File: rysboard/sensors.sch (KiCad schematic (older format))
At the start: 11 parts, among them J11 PICO_BLADE_5, J13 PICO_BLADE_5, J2 PICO_BLADE_5, J3 PICO_BLADE_5, J4 PICO_BLADE_7, J5 PICO_BLADE_5, J6 PICO_BLADE_5, J7 PICO_BLADE_5, J9 PICO_BLADE_5

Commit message: rysboard: schematic cleanup done after kicad import
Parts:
- removed J11, J13, J2, J3, J6, J7, J9: PICO_BLADE_5, symbol rysboard:PICO_BLADE_5
- removed J4: PICO_BLADE_7, symbol rysboard:PICO_BLADE_7
- removed R1, R2: 10k, symbol rysboard:R--rys_PCB-SchDoc-rescue-rysboard-rescue
- added J10: ToF3, Connector_Molex:Molex_PicoBlade_53047-0510_1x05_P1.25mm_Vertical, symbol Connector_Generic:Conn_01x05
- added J11: ToF4, Connector_Molex:Molex_PicoBlade_53047-0510_1x05_P1.25mm_Vertical, symbol Connector_Generic:Conn_01x05
- added J12: ToF5, Connector_Molex:Molex_PicoBlade_53047-0510_1x05_P1.25mm_Vertical, symbol Connector_Generic:Conn_01x05
- added J13: ToF6, Connector_Molex:Molex_PicoBlade_53047-0510_1x05_P1.25mm_Vertical, symbol Connector_Generic:Conn_01x05
- added J14: SPI, Connector_Molex:Molex_PicoBlade_53047-0710_1x07_P1.25mm_Vertical, symbol Connector_Generic:Conn_01x07
- added J15: Temp, Connector_Molex:Molex_PicoBlade_53047-0510_1x05_P1.25mm_Vertical, symbol Connector_Generic:Conn_01x05
- added J16: IMU, Connector_Molex:Molex_PicoBlade_53047-0510_1x05_P1.25mm_Vertical, symbol Connector_Generic:Conn_01x05
- added J9: ToF2, Connector_Molex:Molex_PicoBlade_53047-0510_1x05_P1.25mm_Vertical, symbol Connector_Generic:Conn_01x05
- J8: renamed from J5; value PICO_BLADE_5 -> ToF1; footprint (none) -> Connector_Molex:Molex_PicoBlade_53047-0510_1x05_P1.25mm_Vertical; symbol rysboard:PICO_BLADE_5 -> Connector_Generic:Conn_01x05
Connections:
- net labels added: +3V3, I2C1_CLK, I2C1_SDA, I2C2_CLK, I2C2_SDA, IMU_IRQ, SPI_CLK, SPI_CS, SPI_IRQ, SPI_MISO, SPI_MOSI, TOF1_EN, TOF2_EN, TOF3_EN, TOF4_EN, TOF5_EN, TOF6_EN
- net labels removed: 3V3, BUSY, CE1, FLAG, IRQ, MISO, MOSI, O~D~, SCL, SCL1, SCLK, SDA, SDA1, TOF0, TOF1, TOF2, TOF3, TOF4, TOF5
- wire segments 70 -> 76
- no-connect marks 0 -> 1
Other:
- note added: "6x ToF I2C connector"
- note added: "External SPI connector"
- note added: "I2C IMU connector"
- note added: "I2C temperature sensor connector"
- note removed: "Złącze I2C IMU"
- note removed: "Złącze I2C TEMP"
- note removed: "Złącze I2C ToF 6x"
- note removed: "Złącze SPI"

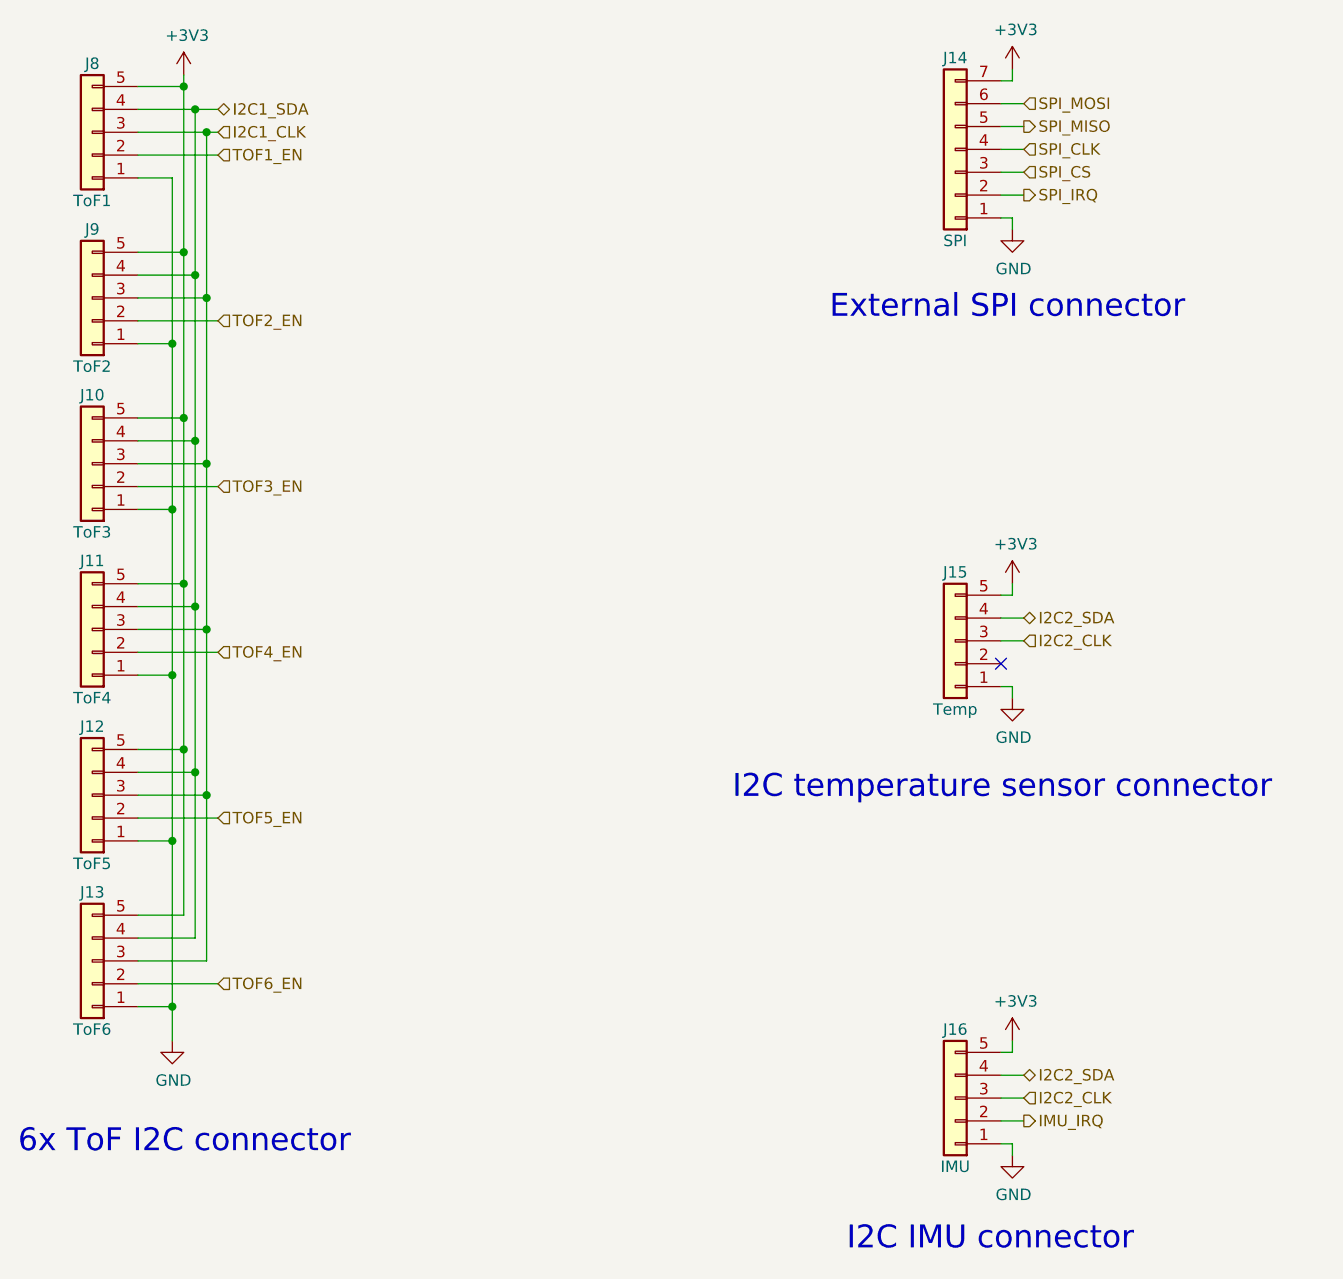
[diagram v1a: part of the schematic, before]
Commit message: rysboard: 4.2 schematic
Change the I2C buses and GPIOs used
Fix L6470 connections
Change ADC to 4-channel
Add 2 user LEDs
Add I2C pullups
Add serial connector
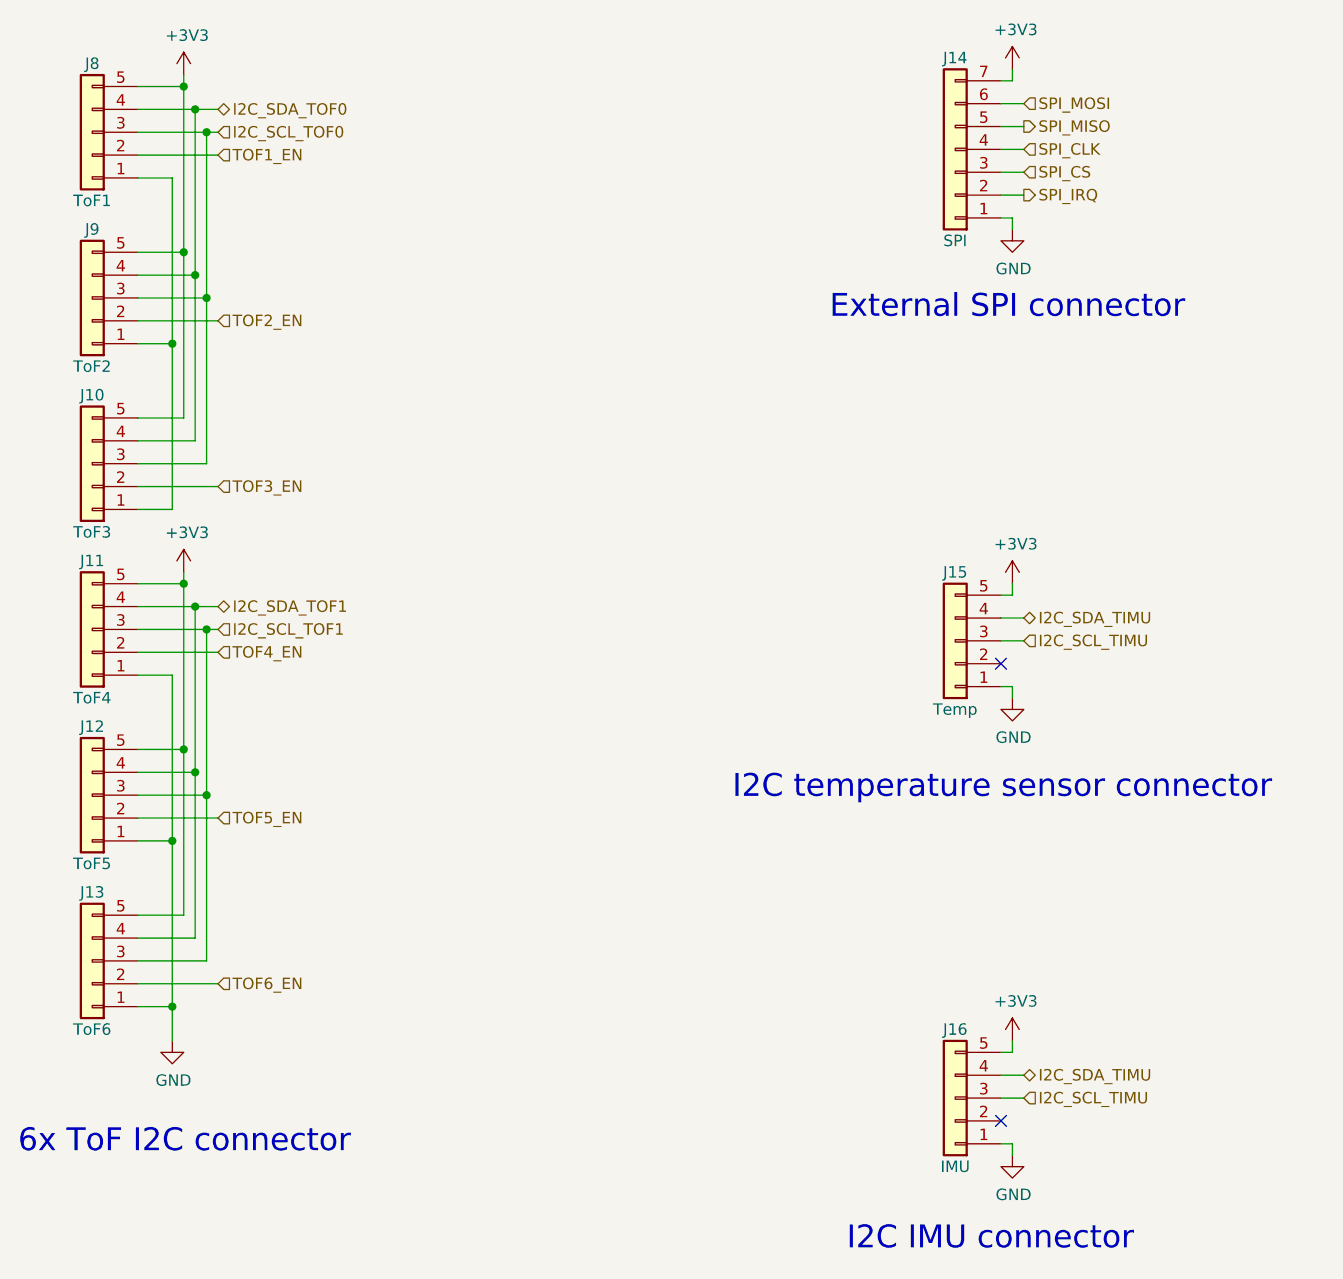
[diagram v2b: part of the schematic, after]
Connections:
- net GND: no longer J10.1 (Pin_1), J8.1 (Pin_1), J9.1 (Pin_1)
- net I2C1_CLK renamed I2C_SCL_TOF0
- net I2C_SCL_TOF0: no longer J11.3 (Pin_3), J12.3 (Pin_3), J13.3 (Pin_3)
- net I2C1_SDA renamed I2C_SDA_TOF0
- net I2C_SDA_TOF0: no longer J11.4 (Pin_4), J12.4 (Pin_4), J13.4 (Pin_4)
- net I2C2_CLK renamed I2C_SCL_TIMU
- net I2C2_SDA renamed I2C_SDA_TIMU
- net IMU_IRQ: no longer names the net of J16.2 (Pin_2)
- new net: J10.1 (Pin_1), J8.1 (Pin_1), J9.1 (Pin_1)
- new net I2C_SCL_TOF1: J11.3 (Pin_3), J12.3 (Pin_3), J13.3 (Pin_3)
- new net I2C_SDA_TOF1: J11.4 (Pin_4), J12.4 (Pin_4), J13.4 (Pin_4)
- no-connect marks 1 -> 2
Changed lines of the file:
@@
 Wire Wire Line
 	2175 3750 2175 4475
-Connection ~ 2175 3750
-Wire Wire Line
-	2175 3025 2175 3750
-Connection ~ 2175 3025
 Wire Wire Line
 	2175 2300 2175 3025
@@
 	1975 3425 2125 3425
 Wire Wire Line
-	2125 3425 2125 4150
-Connection ~ 2125 4150
-Wire Wire Line
 	1975 2700 2125 2700
 Wire Wire Line
 	2125 2700 2125 3425
-Connection ~ 2125 3425
 Wire Wire Line
 	1975 1975 2125 1975
@@
 TOF1_EN
 Text HLabel 2325 1775 2    50   Input ~ 0
-I2C1_CLK
+I2C_SCL_TOF0
 Text HLabel 2325 1675 2    50   BiDi ~ 0
-I2C1_SDA
+I2C_SDA_TOF0
 Wire Wire Line
 	1975 1875 2325 1875
@@
 Wire Wire Line
 	2225 4575 2225 3850
-Connection ~ 2225 3850
-Wire Wire Line
-	2225 3850 2225 3125
-Connection ~ 2225 3125
 Wire Wire Line
 	2225 2400 2225 3125
@@
 Wire Wire Line
 	2275 2500 2275 3225
-Connection ~ 2275 3225
-Wire Wire Line
-	2275 3225 2275 3950
-Connection ~ 2275 3950
 Wire Wire Line
 	2275 4675 2275 3950
@@
 $EndComp
 Text HLabel 5850 4000 2    50   Input ~ 0
-I2C2_CLK
+I2C_SCL_TIMU
 Text HLabel 5850 3900 2    50   BiDi ~ 0
-I2C2_SDA
+I2C_SDA_TIMU
 $Comp
 L power:+3V3 #PWR027
@@
 $EndComp
 Text HLabel 5850 6000 2    50   Input ~ 0
-I2C2_CLK
+I2C_SCL_TIMU
 Text HLabel 5850 5900 2    50   BiDi ~ 0
-I2C2_SDA
+I2C_SDA_TIMU
 $Comp
 L power:+3V3 #PWR029
@@
 Wire Wire Line
 	5750 5900 5850 5900
-Wire Wire Line
-	5750 6100 5850 6100
-Text HLabel 5850 6100 2    50   Output ~ 0
-IMU_IRQ
+Text HLabel 2325 3950 2    50   Input ~ 0
+I2C_SCL_TOF1
+Text HLabel 2325 3850 2    50   BiDi ~ 0
+I2C_SDA_TOF1
+$Comp
+L power:+3V3 #PWR0109
+U 1 1 5E9EC114
+P 2175 3700
+F 0 "#PWR0109" H 2175 3550 50  0001 C CNN
+F 1 "+3V3" H 2190 3873 50  0000 C CNN
+F 2 "" H 2175 3700 50  0001 C CNN
+F 3 "" H 2175 3700 50  0001 C CNN
+	1    2175 3700
+	1    0    0    -1
+$EndComp
+Wire Wire Line
+	2175 3750 2175 3700
+Connection ~ 2175 3750
+Wire Wire Line
+	2225 3850 2325 3850
+Connection ~ 2225 3850
+Wire Wire Line
+	2275 3950 2325 3950
+Connection ~ 2275 3950
+NoConn ~ 5750 6100
 $EndSCHEMATC

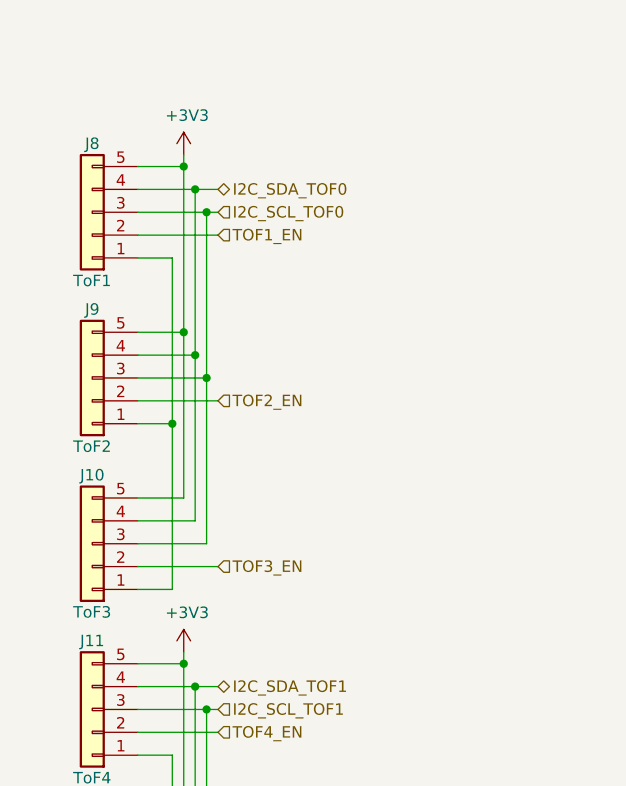
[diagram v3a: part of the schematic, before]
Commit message: rysboard v4.2: * route the whole board (TODO: ground fills, track width checks) * fix half of ToF connectors missing ground connection * swap LEDs for easier routing
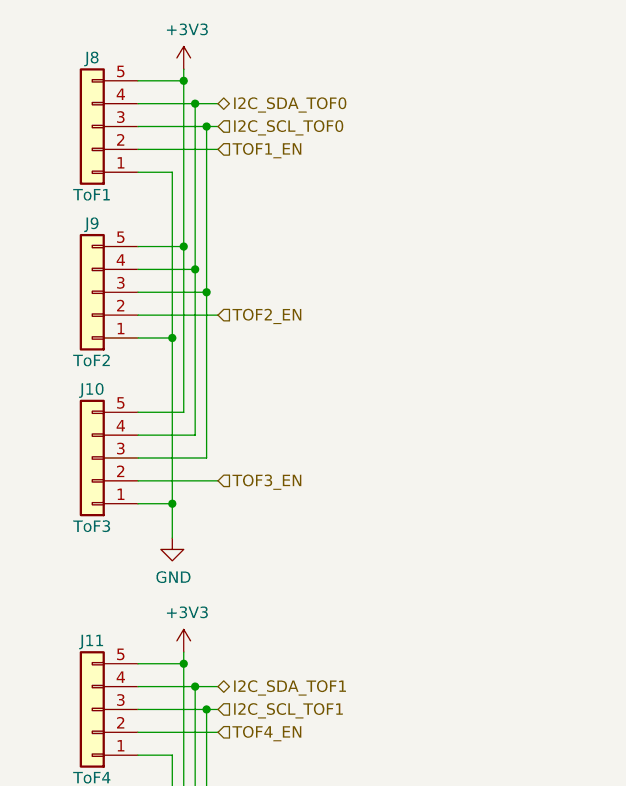
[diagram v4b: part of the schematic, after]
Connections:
- net GND: now also J10.1 (Pin_1), J8.1 (Pin_1), J9.1 (Pin_1)
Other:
- moved on the sheet: J10, J8, J9
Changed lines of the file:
@@
 L Connector_Generic:Conn_01x05 J8
 U 1 1 5EB6D871
-P 1775 1775
-F 0 "J8" H 1775 1475 50  0000 C CNN
-F 1 "ToF1" H 1775 2075 50  0000 C CNN
-F 2 "Connector_Molex:Molex_PicoBlade_53047-0510_1x05_P1.25mm_Vertical" H 1775 1775 50  0001 C CNN
-F 3 "~" H 1775 1775 50  0001 C CNN
-	1    1775 1775
-	-1   0    0    1
-$EndComp
-Wire Wire Line
-	1975 1575 2175 1575
-Wire Wire Line
-	2175 1575 2175 1525
+P 1775 1400
+F 0 "J8" H 1775 1100 50  0000 C CNN
+F 1 "ToF1" H 1775 1700 50  0000 C CNN
+F 2 "Connector_Molex:Molex_PicoBlade_53047-0510_1x05_P1.25mm_Vertical" H 1775 1400 50  0001 C CNN
+F 3 "~" H 1775 1400 50  0001 C CNN
+	1    1775 1400
+	-1   0    0    1
+$EndComp
+Wire Wire Line
+	1975 1200 2175 1200
+Wire Wire Line
+	2175 1200 2175 1150
 $Comp
 L power:+3V3 #PWR024
 U 1 1 5ED4B7A8
-P 2175 1525
-F 0 "#PWR024" H 2175 1375 50  0001 C CNN
-F 1 "+3V3" H 2190 1698 50  0000 C CNN
-F 2 "" H 2175 1525 50  0001 C CNN
-F 3 "" H 2175 1525 50  0001 C CNN
-	1    2175 1525
+P 2175 1150
+F 0 "#PWR024" H 2175 1000 50  0001 C CNN
+F 1 "+3V3" H 2190 1323 50  0000 C CNN
+F 2 "" H 2175 1150 50  0001 C CNN
+F 3 "" H 2175 1150 50  0001 C CNN
+	1    2175 1150
 	1    0    0    -1
 $EndComp
@@
 L Connector_Generic:Conn_01x05 J9
 U 1 1 5ED64AFD
-P 1775 2500
-F 0 "J9" H 1775 2200 50  0000 C CNN
-F 1 "ToF2" H 1775 2800 50  0000 C CNN
-F 2 "Connector_Molex:Molex_PicoBlade_53047-0510_1x05_P1.25mm_Vertical" H 1775 2500 50  0001 C CNN
-F 3 "~" H 1775 2500 50  0001 C CNN
-	1    1775 2500
-	-1   0    0    1
-$EndComp
-Wire Wire Line
-	1975 2300 2175 2300
+P 1775 2125
+F 0 "J9" H 1775 1825 50  0000 C CNN
+F 1 "ToF2" H 1775 2425 50  0000 C CNN
+F 2 "Connector_Molex:Molex_PicoBlade_53047-0510_1x05_P1.25mm_Vertical" H 1775 2125 50  0001 C CNN
+F 3 "~" H 1775 2125 50  0001 C CNN
+	1    1775 2125
+	-1   0    0    1
+$EndComp
+Wire Wire Line
+	1975 1925 2175 1925
 $Comp
 L Connector_Generic:Conn_01x05 J10
 U 1 1 5ED67D31
-P 1775 3225
-F 0 "J10" H 1775 2925 50  0000 C CNN
-F 1 "ToF3" H 1775 3525 50  0000 C CNN
-F 2 "Connector_Molex:Molex_PicoBlade_53047-0510_1x05_P1.25mm_Vertical" H 1775 3225 50  0001 C CNN
-F 3 "~" H 1775 3225 50  0001 C CNN
-	1    1775 3225
-	-1   0    0    1
-$EndComp
-Wire Wire Line
-	1975 3025 2175 3025
+P 1775 2850
+F 0 "J10" H 1775 2550 50  0000 C CNN
+F 1 "ToF3" H 1775 3150 50  0000 C CNN
+F 2 "Connector_Molex:Molex_PicoBlade_53047-0510_1x05_P1.25mm_Vertical" H 1775 2850 50  0001 C CNN
+F 3 "~" H 1775 2850 50  0001 C CNN
+	1    1775 2850
+	-1   0    0    1
+$EndComp
+Wire Wire Line
+	1975 2650 2175 2650
 $Comp
 L Connector_Generic:Conn_01x05 J11
@@
 	2175 3750 2175 4475
 Wire Wire Line
-	2175 2300 2175 3025
-Connection ~ 2175 2300
-Wire Wire Line
-	2175 1575 2175 2300
-Connection ~ 2175 1575
+	2175 1925 2175 2650
+Connection ~ 2175 1925
+Wire Wire Line
+	2175 1200 2175 1925
+Connection ~ 2175 1200
 Wire Wire Line
 	1975 5600 2125 5600
@@
 Connection ~ 2125 4875
 Wire Wire Line
-	1975 3425 2125 3425
-Wire Wire Line
-	1975 2700 2125 2700
-Wire Wire Line
-	2125 2700 2125 3425
-Wire Wire Line
-	1975 1975 2125 1975
-Wire Wire Line
-	2125 1975 2125 2700
-Connection ~ 2125 2700
+	1975 3050 2125 3050
+Wire Wire Line
+	1975 2325 2125 2325
+Wire Wire Line
+	2125 2325 2125 3050
+Wire Wire Line
+	1975 1600 2125 1600
+Wire Wire Line
+	2125 1600 2125 2325
+Connection ~ 2125 2325
 Text HLabel 2325 5500 2    50   Input ~ 0
 TOF6_EN
@@
 	1975 3850 2225 3850
 Wire Wire Line
-	1975 3325 2325 3325
-Wire Wire Line
-	1975 3225 2275 3225
-Wire Wire Line
-	1975 3125 2225 3125
-Text HLabel 2325 2600 2    50   Input ~ 0
+	1975 2950 2325 2950
+Wire Wire Line
+	1975 2850 2275 2850
+Wire Wire Line
+	1975 2750 2225 2750
+Text HLabel 2325 2225 2    50   Input ~ 0
 TOF2_EN
 Wire Wire Line
-	1975 2600 2325 2600
-Wire Wire Line
-	1975 2500 2275 2500
-Wire Wire Line
-	1975 2400 2225 2400
-Text HLabel 2325 1875 2    50   Input ~ 0
+	1975 2225 2325 2225
+Wire Wire Line
+	1975 2125 2275 2125
+Wire Wire Line
+	1975 2025 2225 2025
+Text HLabel 2325 1500 2    50   Input ~ 0
 TOF1_EN
-Text HLabel 2325 1775 2    50   Input ~ 0
+Text HLabel 2325 1400 2    50   Input ~ 0
 I2C_SCL_TOF0
-Text HLabel 2325 1675 2    50   BiDi ~ 0
+Text HLabel 2325 1300 2    50   BiDi ~ 0
 I2C_SDA_TOF0
 Wire Wire Line
-	1975 1875 2325 1875
-Wire Wire Line
-	1975 1775 2275 1775
-Wire Wire Line
-	1975 1675 2225 1675
+	1975 1500 2325 1500
+Wire Wire Line
+	1975 1400 2275 1400
+Wire Wire Line
+	1975 1300 2225 1300
 Wire Wire Line
 	2225 5300 2225 4575
@@
 	2225 4575 2225 3850
 Wire Wire Line
-	2225 2400 2225 3125
-Connection ~ 2225 2400
-Wire Wire Line
-	2225 2400 2225 1675
-Connection ~ 2225 1675
-Wire Wire Line
-	2225 1675 2325 1675
-Wire Wire Line
-	2275 1775 2275 2500
-Connection ~ 2275 1775
-Wire Wire Line
-	2275 1775 2325 1775
-Connection ~ 2275 2500
-Wire Wire Line
-	2275 2500 2275 3225
+	2225 2025 2225 2750
+Connection ~ 2225 2025
+Wire Wire Line
+	2225 2025 2225 1300
+Connection ~ 2225 1300
+Wire Wire Line
+	2225 1300 2325 1300
+Wire Wire Line
+	2275 1400 2275 2125
+Connection ~ 2275 1400
+Wire Wire Line
+	2275 1400 2325 1400
+Connection ~ 2275 2125
+Wire Wire Line
+	2275 2125 2275 2850
 Wire Wire Line
 	2275 4675 2275 3950
@@
 Wire Wire Line
 	2275 4675 2275 5400
-Text HLabel 2325 3325 2    50   Input ~ 0
+Text HLabel 2325 2950 2    50   Input ~ 0
 TOF3_EN
 $Comp
@@
 Connection ~ 2275 3950
 NoConn ~ 5750 6100
+Wire Wire Line
+	2125 3050 2125 3200
+$Comp
+L power:GND #PWR0110
+U 1 1 5F0EBE1A
+P 2125 3200
+F 0 "#PWR0110" H 2125 2950 50  0001 C CNN
+F 1 "GND" H 2130 3027 50  0000 C CNN
+F 2 "" H 2125 3200 50  0001 C CNN
+F 3 "" H 2125 3200 50  0001 C CNN
+	1    2125 3200
+	1    0    0    -1
+$EndComp
+Connection ~ 2125 3050
 $EndSCHEMATC
